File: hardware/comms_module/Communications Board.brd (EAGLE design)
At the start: 33.5 x 32.4 mm, 74 parts, among them U1 Value, U2 STC3115, X2 USB-MICROB, Y1 32.768kHz, Y2 24MHz

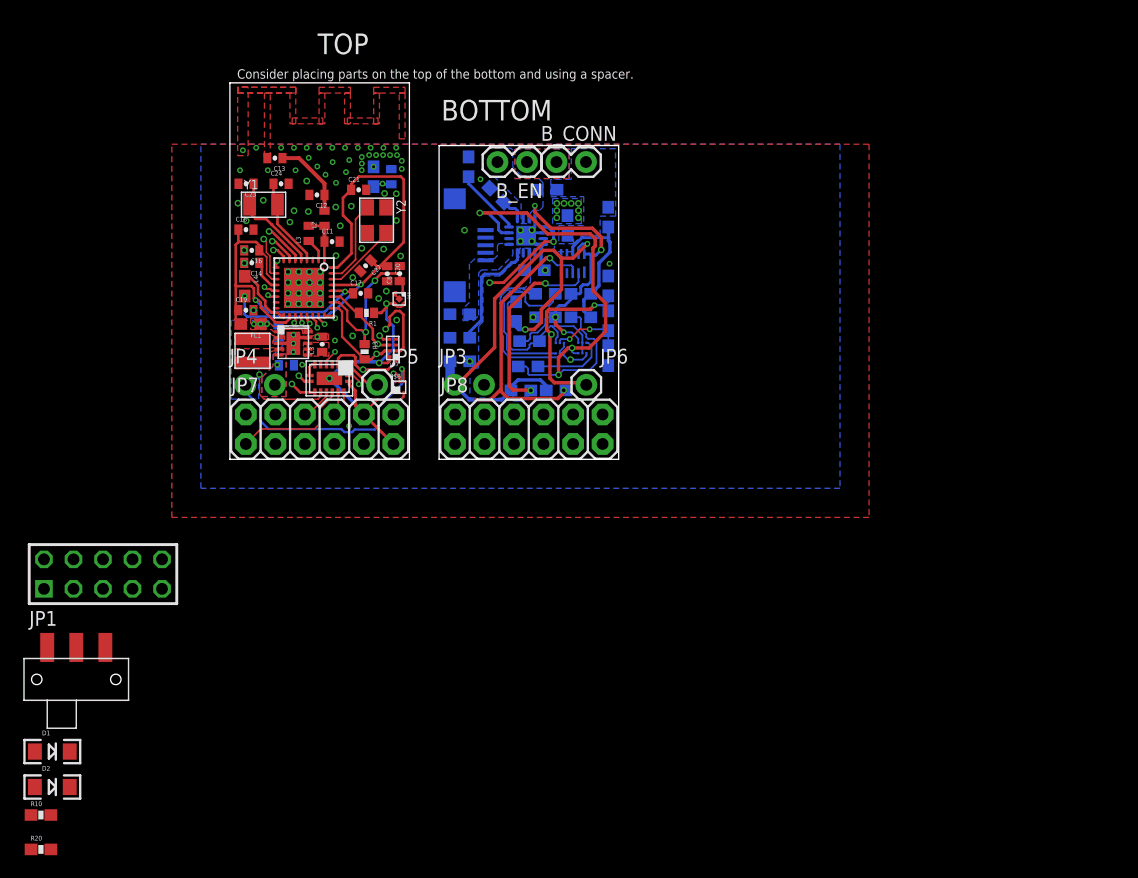
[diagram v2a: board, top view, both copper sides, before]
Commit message: Add programming attachment board.
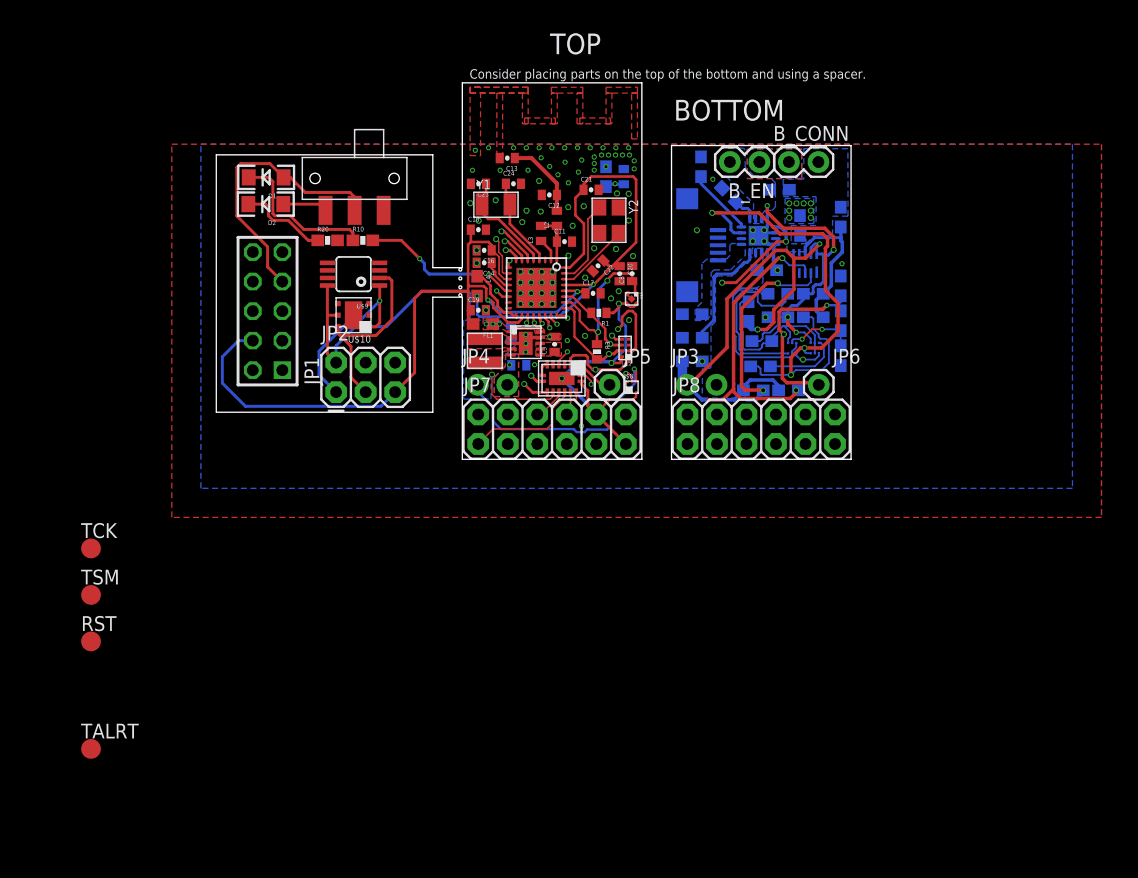
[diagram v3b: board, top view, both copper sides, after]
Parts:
- added JP2: FEMALE 2x3, SparkFun-Connectors:2X3
- added RST, TALRT, TCK, TSM: TPTP17R, testpad:TP17R
- added U$10: HDC1050, Capstone Library:SON-6
- added U$9: MCP9808, Capstone Library:MSOP8
- moved R20 57.9 mm to (8.41, 18.8)
- moved R10 56.7 mm to (11.4, 18.8)
- moved D2 53.4 mm to (3.09, 22.0), turned to 180 degrees
- moved D1 52.7 mm to (3.12, 24.3), turned to 180 degrees
- moved S1 49.3 mm to (10.7, 24.2), turned to 180 degrees
- moved JP1 26.7 mm to (3.24, 12.8), turned to 90 degrees
- moved B_EN 20.0 mm to (45.6, 25.6)
- moved C4 20.0 mm to (46.2, 16.3)
- moved R17 20.0 mm to (50.2, 14.2)
- moved R19 20.0 mm to (44.6, 12.7)
- moved R6 20.0 mm to (50.2, 12.2)
- moved U$2 20.0 mm to (45.5, 19.2)
- moved B_CONN 20.0 mm to (48.1, 25.6)
- moved C1 20.0 mm to (24.9, 8.09)
- moved C10 20.0 mm to (39.8, 8.43)
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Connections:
- new net N$17: JP2.4
- new net N$25: JP2.6
- new net TALRT: TALRT.TP, U$9.3
- net +3V3: now also JP2.2, U$10.5, U$9.8
- net GND: now also U$10.2, U$9.4, U$9.5, U$9.6, U$9.7
- net JTAG_TCKC: now also TCK.TP
- net JTAG_TSMC: now also TSM.TP
- net MCU_RST: now also RST.TP
- net SCL: now also JP2.3, U$10.6, U$9.2
- net SDA: now also JP2.1, U$10.1, U$9.1
- net VCC: now also JP2.5
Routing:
- net VCC: track 47.3 -> 82.6 mm
- net +3V3: track 65.7 -> 91.4 mm
- net PROG_VCC: track 0.00 -> 24.0 mm
- net JTAG_TCKC: track 0.75 -> 23.7 mm
- net JTAG_TSMC: track 1.15 -> 21.4 mm
- net SCL: track 37.8 -> 53.9 mm
- net SDA: track 28.8 -> 44.2 mm, vias 3 -> 4
- net N$14: track 0.00 -> 13.2 mm
- net GND: track 13.6 -> 24.0 mm, vias 98 -> 99
- net N$16: track 0.00 -> 7.70 mm
- net N$6: track 0.00 -> 3.86 mm
- net MCU_RST: track 29.5 -> 27.9 mm
- net MPSW: track 22.3 -> 21.3 mm
- net MSW_0: track 23.6 -> 24.2 mm
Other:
- board size 33.5 x 32.4 mm -> 54.6 x 32.4 mm

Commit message: Complete programming/debug attachment board.
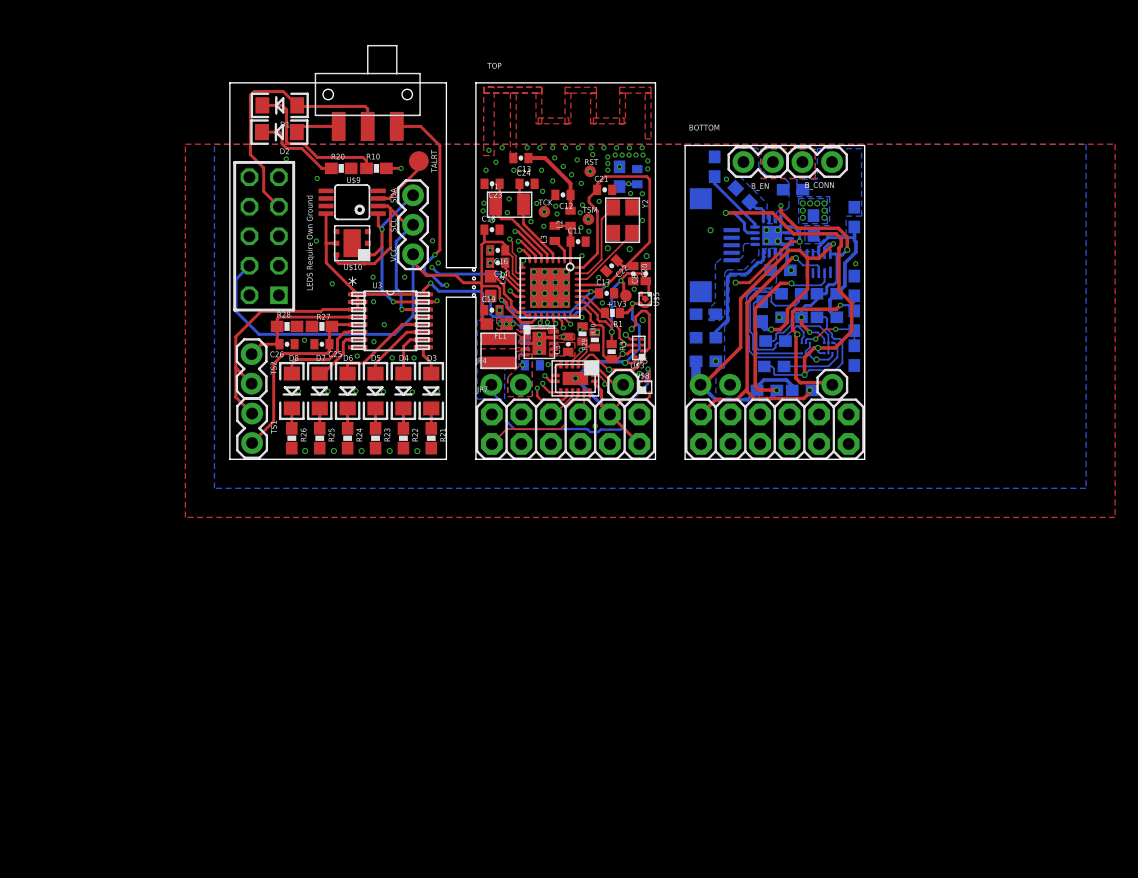
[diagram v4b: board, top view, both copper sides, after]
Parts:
- added +1V3: TPTP10R, testpad:TP10R
- added C25, C26: 100nF, SparkFun-Passives:0402-CAP
- added D3, D4, D5, D6, D7, D8: Green, SparkFun-LED:LED-1206
- added R21, R22, R23, R24, R25, R26: 180, SparkFun-Passives:0603-RES
- added R27, R28: 10k, SparkFun-Passives:0603-RES
- added R29, R30: 1Meg, SparkFun-Passives:0402-RES
- added TS1, TS2: (no value), SparkFun-Connectors:1X02
- added U3: TCA9554A_PW_16, Capstone Library:PW16
- JP2: value FEMALE 2x3 -> (none); device SparkFun-Connectors:2X3 -> SparkFun-Connectors:1X03
- RST, TCK, TSM: value TPTP17R -> TPTP10R; device testpad:TP17R -> testpad:TP10R
- moved RST 59.0 mm to (31.0, 24.8)
- moved TALRT 57.9 mm to (16.3, 25.7)
- moved TSM 53.6 mm to (30.9, 20.7)
- moved TCK 48.6 mm to (27.1, 21.3)
- moved JP2 13.6 mm to (15.8, 17.6), turned to 90 degrees
- moved S1 7.31 mm to (11.9, 31.4)
- moved JP1 6.45 mm to (2.95, 19.2)
- moved R10 6.30 mm to (12.6, 25.0)
- moved R20 6.30 mm to (9.58, 25.0)
- moved D1 6.30 mm to (4.29, 30.5)
- moved D2 6.30 mm to (4.26, 28.2)
- moved U$9 6.19 mm to (10.5, 22.1)
- moved U$10 6.19 mm to (10.5, 18.6)
- moved R3 1.26 mm to (32.9, 9.26)
- moved B_CONN 1.17 mm to (49.3, 25.6)
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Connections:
- removed net DBG_LED: U$1.4
- removed net N$25: JP2.6
- new net N$11: C25.1, R27.1, TS1.1, U3.5
- new net N$13: D4.A, U3.10
- new net N$15: D5.A, U3.11
- new net N$28: D8.A, U3.6
- new net N$29: D7.A, U3.7
- new net N$30: D3.C, R21.1
- new net N$31: D4.C, R22.1
- new net N$32: D5.C, R23.1
- new net N$33: D6.C, R24.1
- new net N$34: D7.C, R25.1
- new net N$35: D8.C, R26.1
- new net N$36: C26.1, R28.1, TS2.1, U3.4
- new net N$7: D3.A, U3.9
- new net V_PREBUCK_DIV2: R29.1, R30.2, U$1.4
- net +1V3: now also +1V3.TP
- net +3V3: now also TS1.2, TS2.2, U3.1, U3.16, U3.2, U3.3; no longer JP2.2
- net GND: now also C25.2, C26.2, R21.2, R22.2, R23.2, R24.2, R25.2, R26.2, R27.2, R28.2, R30.1, U3.8
- net N$17: now also D6.A, U3.12; no longer JP2.4
- net SCL: now also JP2.2, U3.14; no longer JP2.3
- net SDA: now also JP2.3, U3.15; no longer JP2.1
- net VCC: now also JP2.1; no longer JP2.5
- net V_PREBUCK: now also R29.2
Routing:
- net V_PREBUCK: track 8.90 -> 48.7 mm, vias 3 -> 6
- net MCU_RST: track 27.9 -> 56.9 mm, vias 2 -> 5
- net SCL: track 53.9 -> 79.0 mm, vias 3 -> 4
- net SDA: track 44.2 -> 64.8 mm, vias 4 -> 6
- net +3V3: track 91.4 -> 110.8 mm, vias 6 -> 7
- net N$11: track 0.00 -> 17.3 mm
- net JTAG_TSMC: track 21.4 -> 34.8 mm, vias 1 -> 3
- net N$36: track 0.00 -> 12.0 mm
- net N$17: track 0.00 -> 8.74 mm
- net N$28: track 0.00 -> 8.25 mm
- net JTAG_TCKC: track 23.7 -> 31.8 mm, vias 1 -> 2
- net N$15: track 0.00 -> 6.10 mm
- net TALRT: track 0.00 -> 5.21 mm
- net N$29: track 0.00 -> 5.04 mm
- net N$13: track 0.00 -> 4.27 mm
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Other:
- outline, holes or cut-outs redrawn
- board text added: "LEDS Require Own Ground"
- board text added: "SCL"
- board text added: "SDA"
- board text added: "VCC"
- board text removed: "Consider placing parts on the top of the bottom and using a spacer."

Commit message: Create muiltiple schematic sheets, and organize
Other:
- board text added: "Debug Attachment Board"
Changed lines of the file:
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@@
 <layer number="17" name="Pads" color="2" fill="1" visible="yes" active="yes"/>
 <layer number="18" name="Vias" color="2" fill="1" visible="yes" active="yes"/>
-<layer number="19" name="Unrouted" color="6" fill="1" visible="yes" active="yes"/>
+<layer number="19" name="Unrouted" color="6" fill="1" visible="no" active="yes"/>
 <layer number="20" name="Dimension" color="15" fill="1" visible="yes" active="yes"/>
 <layer number="21" name="tPlace" color="7" fill="1" visible="yes" active="yes"/>
@@
 <wire x1="54.62" y1="0" x2="54.62" y2="27" width="0" layer="20"/>
 <wire x1="39.17" y1="27" x2="54.62" y2="27" width="0" layer="20"/>
-<text x="22.15" y="33.61" size="0.5" layer="21" ratio="11">TOP</text>
-<text x="39.49" y="28.29" size="0.5" layer="21" ratio="11">BOTTOM</text>
-<polygon width="0.3048" layer="39">
-<vertex x="20.94" y="32.8021"/>
-<vertex x="20.93" y="27.1121"/>
-<vertex x="37.17" y="27.1121"/>
-<vertex x="37.17" y="32.8021"/>
-</polygon>
-<polygon width="0.3048" layer="40">
-<vertex x="20.92" y="32.8021"/>
-<vertex x="20.93" y="27.1121"/>
-<vertex x="37.17" y="27.1121"/>
-<vertex x="37.17" y="32.8021"/>
-</polygon>
+<text x="28.39" y="-1.81" size="0.5" layer="21" ratio="11">TOP</text>
+<text x="45.05" y="-1.73" size="0.5" layer="21" ratio="11">BOTTOM</text>
 <text x="21.6" y="38.19" size="0.5" layer="51" ratio="11">Note: The distance from the top of the antenna to
  the board edge is increased due to the
@@
 <text x="14.33" y="22.05" size="0.5" layer="25" ratio="11" rot="R90">SDA</text>
 <text x="14.33" y="17" size="0.5" layer="25" ratio="11" rot="R90">VCC</text>
+<text x="6.15" y="-1.93" size="0.5" layer="21" ratio="11">Debug Attachment Board</text>
 </plain>
 <attributes>
@@
 <attribute name="PROD_ID" value="CONN-12423" x="22.54" y="1.32" size="1.778" layer="27" display="off"/>
 <attribute name="NAME" x="21.27" y="5.765" size="0.5" layer="25" ratio="11"/>
-<attribute name="VALUE" x="21.27" y="-1.855" size="0.5" layer="27" ratio="11"/>
 </element>
 <element name="JP8" library="SparkFun-Connectors" package="2X6" value="2X6 FEMALE" x="40.54" y="1.32" smashed="yes">
 <attribute name="PROD_ID" value="CONN-12423" x="40.54" y="1.32" size="1.778" layer="27" display="off"/>
-<attribute name="VALUE" x="39.27" y="-1.855" size="0.5" layer="27" ratio="11"/>
 </element>
 <element name="JP1" library="avr-7" package="AVR-JTAG-10" value="AVR-JTAG-10" x="2.95" y="19.1931" smashed="yes" rot="R90">
